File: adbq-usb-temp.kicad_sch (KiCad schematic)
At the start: 75 parts, among them J4 USB_C_Receptacle_USB2.0_14P, Q1 Q_NMOS, Q2 Q_NMOS, Q3 Q_NMOS, SW1 SW_Push, SW2 TestPoint, SW3 TestPoint, SW4 TestPoint, U1 ESP32-S3FH4R2, U14 TMP117AIDRV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

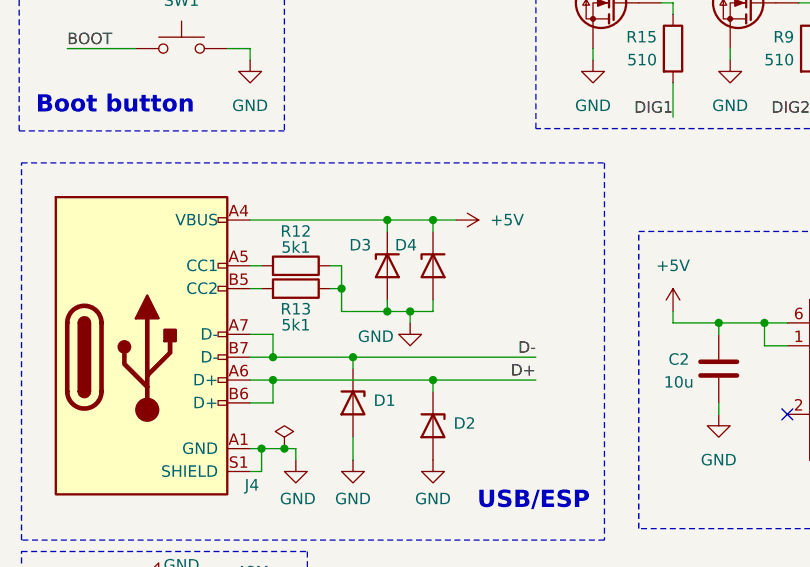
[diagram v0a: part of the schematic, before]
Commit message: pcb: add board outline
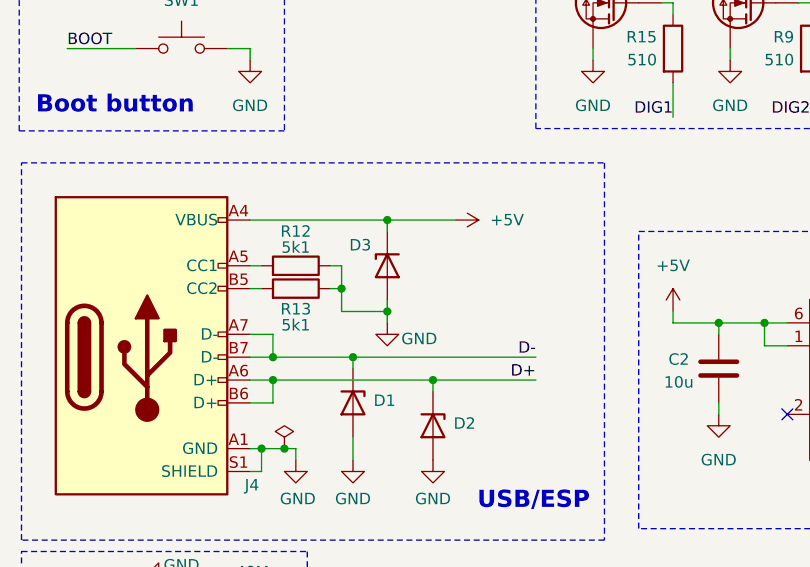
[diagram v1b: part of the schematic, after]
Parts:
- removed D4: H5VU10U, Pers:Diode_DFN1006, symbol Pers:H5VU10U
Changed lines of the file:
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@@
 	)
 	(junction
-		(at 62.23 135.89)
-		(diameter 0)
-		(color 0 0 0 0)
-	)
-	(junction
 		(at 148.59 158.75)
 		(diameter 0)
@@
 	)
 	(junction
-		(at 59.69 146.05)
-		(diameter 0)
-		(color 0 0 0 0)
-	)
-	(junction
 		(at 57.15 146.05)
 		(diameter 0)
@@
 	(wire
 		(pts
-			(xy 59.69 146.05) (xy 62.23 146.05)
-		)
-		(stroke
-			(width 0)
-			(type default)
-		)
-	)
-	(wire
-		(pts
 			(xy 45.72 161.29) (xy 46.99 161.29)
 		)
@@
 	(wire
 		(pts
-			(xy 59.69 147.32) (xy 59.69 146.05)
+			(xy 57.15 147.32) (xy 57.15 146.05)
 		)
 		(stroke
@@
 	(wire
 		(pts
-			(xy 57.15 146.05) (xy 59.69 146.05)
-		)
-		(stroke
-			(width 0)
-			(type default)
-		)
-	)
-	(wire
-		(pts
 			(xy 31.75 190.5) (xy 31.75 189.23)
 		)
@@
 	(wire
 		(pts
-			(xy 62.23 144.78) (xy 62.23 146.05)
-		)
-		(stroke
-			(width 0)
-			(type default)
-		)
-	)
-	(wire
-		(pts
-			(xy 62.23 135.89) (xy 62.23 137.16)
-		)
-		(stroke
-			(width 0)
-			(type default)
-		)
-	)
-	(wire
-		(pts
 			(xy 44.45 156.21) (xy 44.45 153.67)
 		)
@@
 	(wire
 		(pts
-			(xy 62.23 135.89) (xy 64.77 135.89)
-		)
-		(stroke
-			(width 0)
-			(type default)
-		)
-	)
-	(wire
-		(pts
 			(xy 172.72 38.1) (xy 182.88 38.1)
 		)
@@
 	(wire
 		(pts
-			(xy 57.15 135.89) (xy 62.23 135.89)
+			(xy 57.15 135.89) (xy 64.77 135.89)
 		)
 		(stroke
@@
 	)
 	(symbol
-		(lib_id "Pers:H5VU10U")
-		(at 62.23 140.97 90)
-		(mirror x)
-		(unit 1)
-		(exclude_from_sim no)
-		(in_bom yes)
-		(on_board yes)
-		(dnp no)
-		(property "Reference" "D4"
-			(at 60.452 138.684 90)
-			(effects
-				(font
-					(size 1.27 1.27)
-				)
-				(justify left)
-			)
-		)
-		(property "Value" "H5VU10U"
-			(at 59.69 142.2399 90)
-			(effects
-				(font
-					(size 1.27 1.27)
-				)
-				(justify left)
-				(hide yes)
-			)
-		)
-		(property "Footprint" "Pers:Diode_DFN1006"
-			(at 66.675 140.97 0)
-			(effects
-				(font
-					(size 1.27 1.27)
-				)
-				(hide yes)
-			)
-		)
-		(property "Datasheet" "https://datasheet.lcsc.com/lcsc/2504101957_hongjiacheng-H5VU10U_C22395519.pdf"
-			(at 62.23 140.97 0)
-			(effects
-				(font
-					(size 1.27 1.27)
-				)
-				(hide yes)
-			)
-		)
-		(property "Description" "-55℃~+155℃ 0.8pF 16V 200nA 55W@8/20us 5A@8/20us 5V 6V ESD IEC 61000-4-2 Unidirectional DFN1006-2L ESD and Surge Protection (TVS/ESD) ROHS"
-			(at 62.23 140.97 0)
-			(effects
-				(font
-					(size 1.27 1.27)
-				)
-				(hide yes)
-			)
-		)
-		(property "Basic" "E"
-			(at 62.23 140.97 90)
-			(effects
-				(font
-					(size 1.27 1.27)
-				)
-				(hide yes)
-			)
-		)
-		(property "JLCPCB Part #" "C22395519"
-			(at 62.23 140.97 90)
-			(effects
-				(font
-					(size 1.27 1.27)
-				)
-				(hide yes)
-			)
-		)
-		(property "Manufacturer" "hongjiacheng"
-			(at 62.23 140.97 90)
-			(effects
-				(font
-					(size 1.27 1.27)
-				)
-				(hide yes)
-			)
-		)
-		(property "Manufacturer Part Number" "H5VU10U"
-			(at 62.23 140.97 90)
-			(effects
-				(font
-					(size 1.27 1.27)
-				)
-				(hide yes)
-			)
-		)
-		(pin "1"
-		)
-		(pin "2"
-		)
-		(instances
-			(project "adbq-usb-temp"
-				(path "/683f6451-7bb7-4686-955a-dbaefe964302"
-					(reference "D4")
-					(unit 1)
-				)
-			)
-		)
-	)
-	(symbol
 		(lib_id "Switch:SW_Push")
 		(at 34.29 116.84 0)
@@
 	(symbol
 		(lib_id "power:GND")
-		(at 59.69 147.32 0)
+		(at 57.15 147.32 0)
 		(mirror y)
 		(unit 1)
@@
 		(dnp no)
 		(property "Reference" "#PWR029"
-			(at 59.69 153.67 0)
+			(at 57.15 153.67 0)
 			(effects
 				(font
@@
 		)
 		(property "Value" "GND"
-			(at 55.88 148.844 0)
+			(at 60.706 149.098 0)
 			(effects
 				(font
@@
 		)
 		(property "Footprint" ""
-			(at 59.69 147.32 0)
+			(at 57.15 147.32 0)
 			(effects
 				(font
@@
 		)
 		(property "Datasheet" ""
-			(at 59.69 147.32 0)
+			(at 57.15 147.32 0)
 			(effects
 				(font
@@
 		)
 		(property "Description" "Power symbol creates a global label with name \"GND\" , ground"
-			(at 59.69 147.32 0)
+			(at 57.15 147.32 0)
 			(effects
 				(font

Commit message: pcb: add SMPS routing
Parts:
- C2: footprint Capacitor_SMD:C_0402_1005Metric -> Capacitor_SMD:C_0603_1608Metric; JLCPCB Part # C15525 -> C19702; Manufacturer Part Number CL05A106MQ5NUNC -> CL10A106KP8NNNC
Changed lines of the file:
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@@
 			)
 		)
-		(property "Footprint" "Capacitor_SMD:C_0402_1005Metric"
+		(property "Footprint" "Capacitor_SMD:C_0603_1608Metric"
 			(at 94.9452 156.21 0)
 			(effects
@@
 			)
 		)
-		(property "JLCPCB Part #" "C15525"
+		(property "JLCPCB Part #" "C19702"
 			(at 93.98 152.4 0)
 			(effects
@@
 			)
 		)
-		(property "Manufacturer Part Number" "CL05A106MQ5NUNC"
+		(property "Manufacturer Part Number" "CL10A106KP8NNNC"
 			(at 93.98 152.4 0)
 			(effects

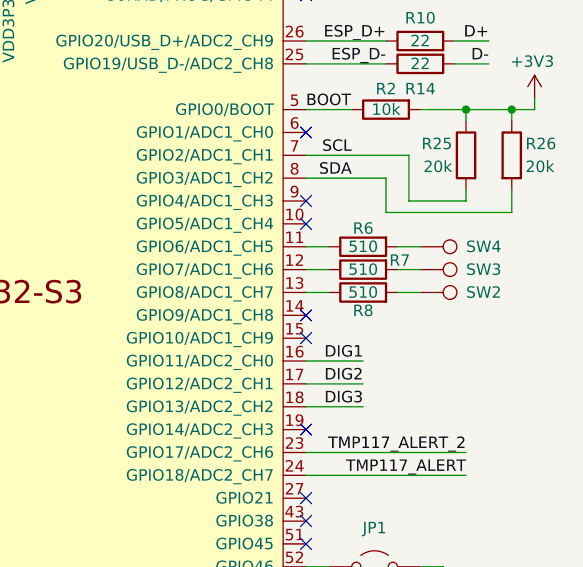
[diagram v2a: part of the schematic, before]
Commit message: pcb: add i2c routing
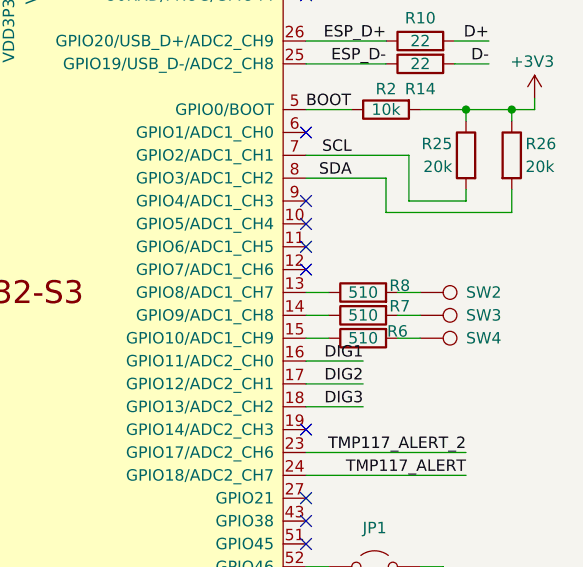
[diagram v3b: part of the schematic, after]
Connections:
- net at R6.1: now also U1.15 (GPIO10/ADC1_CH9); no longer U1.11 (GPIO6/ADC1_CH5)
- net at U1.12 (GPIO7/ADC1_CH6): no longer R7.1
- net at U1.14 (GPIO9/ADC1_CH8): now also R7.1
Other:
- moved on the sheet: R6, R7, SW3, SW4
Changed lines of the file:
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@@
 	)
 	(no_connect
-		(at 232.41 95.25)
-	)
-	(no_connect
 		(at 166.37 92.71)
 	)
@@
 	)
 	(no_connect
-		(at 232.41 97.79)
-	)
-	(no_connect
 		(at 166.37 123.19)
 	)
@@
 	)
 	(no_connect
+		(at 232.41 90.17)
+	)
+	(no_connect
 		(at 232.41 115.57)
 	)
 	(no_connect
+		(at 232.41 87.63)
+	)
+	(no_connect
 		(at 166.37 125.73)
 	)
@@
 	(wire
 		(pts
-			(xy 242.57 92.71) (xy 245.11 92.71)
+			(xy 232.41 95.25) (xy 234.95 95.25)
 		)
 		(stroke
@@
 	(wire
 		(pts
-			(xy 48.26 80.01) (xy 55.88 80.01)
+			(xy 242.57 92.71) (xy 245.11 92.71)
 		)
 		(stroke
@@
 	(wire
 		(pts
-			(xy 53.34 151.13) (xy 53.34 152.4)
+			(xy 48.26 80.01) (xy 55.88 80.01)
 		)
 		(stroke
@@
 	(wire
 		(pts
-			(xy 62.23 153.67) (xy 73.66 153.67)
+			(xy 53.34 151.13) (xy 53.34 152.4)
 		)
 		(stroke
@@
 	(wire
 		(pts
-			(xy 137.16 147.32) (xy 139.7 147.32)
+			(xy 62.23 153.67) (xy 73.66 153.67)
 		)
 		(stroke
@@
 	(wire
 		(pts
-			(xy 129.54 160.02) (xy 129.54 157.48)
+			(xy 137.16 147.32) (xy 139.7 147.32)
 		)
 		(stroke
@@
 	(wire
 		(pts
-			(xy 232.41 90.17) (xy 234.95 90.17)
+			(xy 129.54 160.02) (xy 129.54 157.48)
 		)
 		(stroke
@@
 	(wire
 		(pts
+			(xy 242.57 97.79) (xy 245.11 97.79)
+		)
+		(stroke
+			(width 0)
+			(type default)
+		)
+	)
+	(wire
+		(pts
 			(xy 152.4 107.95) (xy 153.67 107.95)
 		)
@@
 	(wire
 		(pts
-			(xy 242.57 90.17) (xy 245.11 90.17)
-		)
-		(stroke
-			(width 0)
-			(type default)
-		)
-	)
-	(wire
-		(pts
 			(xy 137.16 44.45) (xy 142.24 44.45)
 		)
@@
 	(wire
 		(pts
-			(xy 242.57 87.63) (xy 245.11 87.63)
-		)
-		(stroke
-			(width 0)
-			(type default)
-		)
-	)
-	(wire
-		(pts
 			(xy 41.91 135.89) (xy 57.15 135.89)
 		)
@@
 	(wire
 		(pts
+			(xy 242.57 95.25) (xy 245.11 95.25)
+		)
+		(stroke
+			(width 0)
+			(type default)
+		)
+	)
+	(wire
+		(pts
 			(xy 36.83 185.42) (xy 36.83 186.69)
 		)
@@
 	(wire
 		(pts
-			(xy 232.41 87.63) (xy 234.95 87.63)
-		)
-		(stroke
-			(width 0)
-			(type default)
-		)
-	)
-	(wire
-		(pts
 			(xy 243.84 77.47) (xy 243.84 82.55)
 		)
@@
 	(wire
 		(pts
+			(xy 232.41 97.79) (xy 234.95 97.79)
+		)
+		(stroke
+			(width 0)
+			(type default)
+		)
+	)
+	(wire
+		(pts
 			(xy 166.37 107.95) (xy 161.29 107.95)
 		)
@@
 	(symbol
 		(lib_id "Connector:TestPoint")
-		(at 245.11 90.17 270)
+		(at 245.11 95.25 270)
 		(unit 1)
 		(exclude_from_sim no)
@@
 		(dnp no)
 		(property "Reference" "SW3"
-			(at 250.19 90.17 90)
+			(at 250.19 95.25 90)
 			(effects
 				(font
@@
 		)
 		(property "Value" "TestPoint"
-			(at 250.19 91.4399 90)
+			(at 250.19 96.5199 90)
 			(effects
 				(font
@@
 		)
 		(property "Footprint" "TestPoint:TestPoint_Pad_D1.5mm"
-			(at 245.11 95.25 0)
+			(at 245.11 100.33 0)
 			(effects
 				(font
@@
 		)
 		(property "Datasheet" "~"
-			(at 245.11 95.25 0)
+			(at 245.11 100.33 0)
 			(effects
 				(font
@@
 		)
 		(property "Description" "test point"
-			(at 245.11 90.17 0)
+			(at 245.11 95.25 0)
 			(effects
 				(font
@@
 	(symbol
 		(lib_id "Connector:TestPoint")
-		(at 245.11 87.63 270)
+		(at 245.11 97.79 270)
 		(unit 1)
 		(exclude_from_sim no)
@@
 		(dnp no)
 		(property "Reference" "SW4"
-			(at 250.19 87.63 90)
+			(at 250.19 97.79 90)
 			(effects
 				(font
@@
 		)
 		(property "Value" "TestPoint"
-			(at 250.19 88.8999 90)
+			(at 250.19 99.0599 90)
 			(effects
 				(font
@@
 		)
 		(property "Footprint" "TestPoint:TestPoint_Pad_D1.5mm"
-			(at 245.11 92.71 0)
+			(at 245.11 102.87 0)
 			(effects
 				(font
@@
 		)
 		(property "Datasheet" "~"
-			(at 245.11 92.71 0)
+			(at 245.11 102.87 0)
 			(effects
 				(font
@@
 		)
 		(property "Description" "test point"
-			(at 245.11 87.63 0)
+			(at 245.11 97.79 0)
 			(effects
 				(font
@@
 		(dnp no)
 		(property "Reference" "R8"
-			(at 238.76 94.742 90)
+			(at 242.824 91.948 90)
 			(effects
 				(font
@@
 	(symbol
 		(lib_id "Device:R")
-		(at 238.76 87.63 90)
+		(at 238.76 97.79 90)
 		(mirror x)
 		(unit 1)
@@
 		(dnp no)
 		(property "Reference" "R6"
-			(at 238.76 85.598 90)
+			(at 242.57 97.028 90)
 			(effects
 				(font
@@
 		)
 		(property "Value" "510"
-			(at 238.76 87.63 90)
+			(at 238.76 97.79 90)
 			(effects
 				(font
@@
 		)
 		(property "Footprint" "Resistor_SMD:R_0402_1005Metric"
-			(at 238.76 85.852 90)
+			(at 238.76 96.012 90)
 			(effects
 				(font
@@
 		)
 		(property "Datasheet" "~"
-			(at 238.76 87.63 0)
+			(at 238.76 97.79 0)
 			(effects
 				(font
@@
 		)
 		(property "Description" "Resistor"
-			(at 238.76 87.63 0)
+			(at 238.76 97.79 0)
 			(effects
 				(font
@@
 		)
 		(property "Basic" "Y"
-			(at 238.76 87.63 90)
+			(at 238.76 97.79 90)
 			(effects
 				(font
@@
 		)
 		(property "JLCPCB Part #" "C25123"
-			(at 238.76 87.63 90)
+			(at 238.76 97.79 90)
 			(effects
 				(font
@@
 		)
 		(property "Manufacturer" "Uniroyal Elec"
-			(at 238.76 87.63 90)
+			(at 238.76 97.79 90)
 			(effects
 				(font
@@
 		)
 		(property "Manufacturer Part Number" "0402WGF5100TCE"
-			(at 238.76 87.63 90)
+			(at 238.76 97.79 90)
 			(effects
 				(font
@@
 		)
 		(instances
-			(project ""
+			(project "adbq-usb-temp"
 				(path "/683f6451-7bb7-4686-955a-dbaefe964302"
 					(reference "R6")
@@
 	(symbol
 		(lib_id "Device:R")
-		(at 238.76 90.17 90)
+		(at 238.76 95.25 90)
 		(mirror x)
 		(unit 1)
@@
 		(dnp no)
 		(property "Reference" "R7"
-			(at 242.824 89.154 90)
+			(at 242.824 94.234 90)
 			(effects
 				(font
@@
 		)
 		(property "Value" "510"
-			(at 238.76 90.17 90)
+			(at 238.76 95.25 90)
 			(effects
 				(font
@@
 		)
 		(property "Footprint" "Resistor_SMD:R_0402_1005Metric"
-			(at 238.76 88.392 90)
+			(at 238.76 93.472 90)
 			(effects
 				(font
@@
 		)
 		(property "Datasheet" "~"
-			(at 238.76 90.17 0)
+			(at 238.76 95.25 0)
 			(effects
 				(font
@@
 		)
 		(property "Description" "Resistor"
-			(at 238.76 90.17 0)
+			(at 238.76 95.25 0)
 			(effects
 				(font
@@
 		)
 		(property "Basic" "Y"
-			(at 238.76 90.17 90)
+			(at 238.76 95.25 90)
 			(effects
 				(font
@@
 		)
 		(property "JLCPCB Part #" "C25123"
-			(at 238.76 90.17 90)
+			(at 238.76 95.25 90)
 			(effects
 				(font
@@
 		)
 		(property "Manufacturer" "Uniroyal Elec"
-			(at 238.76 90.17 90)
+			(at 238.76 95.25 90)
 			(effects
 				(font
@@
 		)
 		(property "Manufacturer Part Number" "0402WGF5100TCE"
-			(at 238.76 90.17 90)
+			(at 238.76 95.25 90)
 			(effects
 				(font

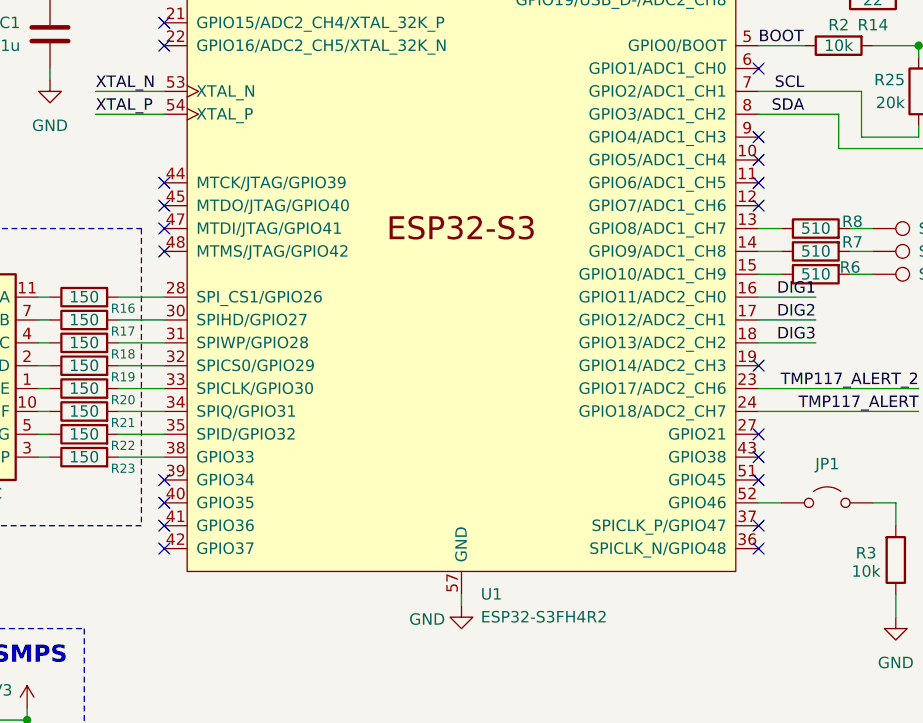
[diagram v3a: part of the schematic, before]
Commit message: pcb: add segment display routing
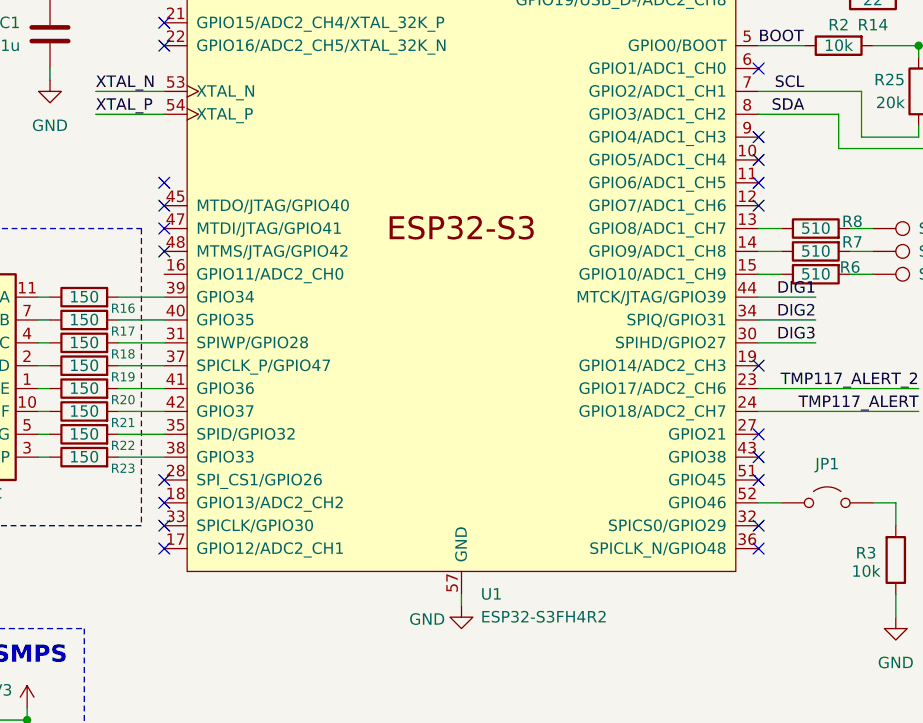
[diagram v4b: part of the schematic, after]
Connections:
- net DIG1: now also U1.44 (MTCK/JTAG/GPIO39); no longer U1.16 (GPIO11/ADC2_CH0)
- net DIG2: now also U1.34 (SPIQ/GPIO31); no longer U1.17 (GPIO12/ADC2_CH1)
- net DIG3: now also U1.30 (SPIHD/GPIO27); no longer U1.18 (GPIO13/ADC2_CH2)
- net at R16.2: now also U1.39 (GPIO34); no longer U1.28 (SPI_CS1/GPIO26)
- net at R17.2: now also U1.40 (GPIO35); no longer U1.30 (SPIHD/GPIO27)
- net at R20.2: now also U1.41 (GPIO36); no longer U1.33 (SPICLK/GPIO30)
- net at R19.2: now also U1.37 (SPICLK_P/GPIO47); no longer U1.32 (SPICS0/GPIO29)
- net at R21.2: now also U1.42 (GPIO37); no longer U1.34 (SPIQ/GPIO31)
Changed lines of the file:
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@@
 		(on_board yes)
 		(dnp no)
-		(fields_autoplaced yes)
 		(property "Reference" "U1"
 			(at 201.5333 133.35 0)

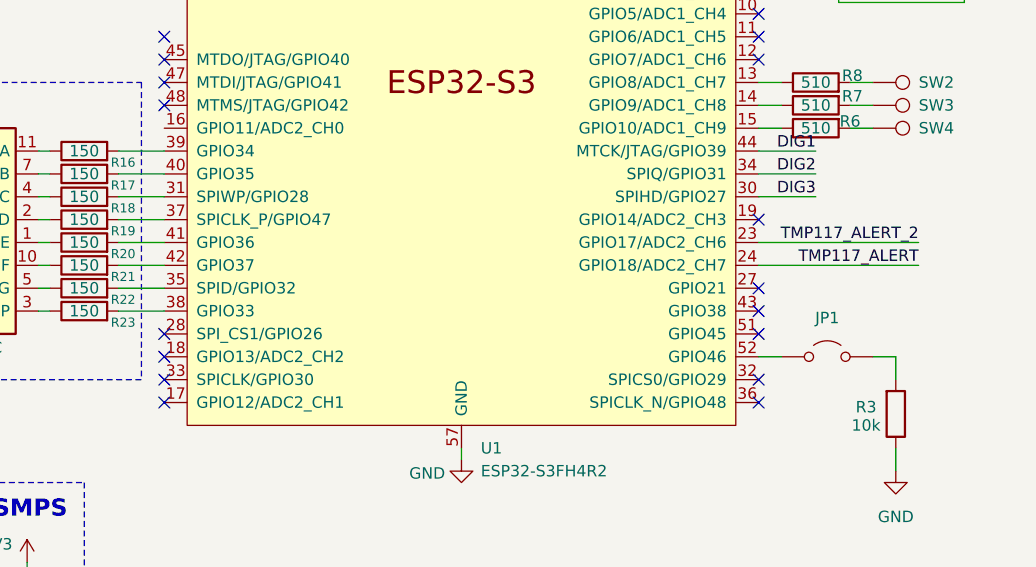
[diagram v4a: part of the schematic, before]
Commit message: pcb: add TMP117 routing
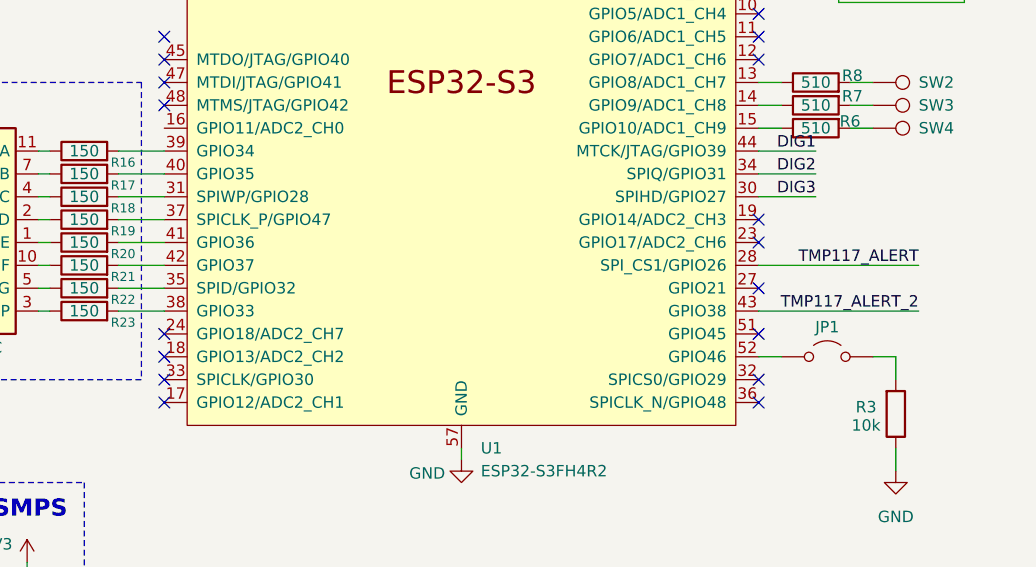
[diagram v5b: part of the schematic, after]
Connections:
- net TMP117_ALERT: now also U1.28 (SPI_CS1/GPIO26); no longer U1.24 (GPIO18/ADC2_CH7)
- net TMP117_ALERT_2: now also U1.43 (GPIO38); no longer U1.23 (GPIO17/ADC2_CH6)
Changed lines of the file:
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@@
 	)
 	(no_connect
-		(at 232.41 118.11)
-	)
-	(no_connect
 		(at 232.41 74.93)
 	)
@@
 	)
 	(no_connect
+		(at 232.41 110.49)
+	)
+	(no_connect
 		(at 166.37 90.17)
 	)
@@
 	(wire
 		(pts
+			(xy 232.41 118.11) (xy 250.19 118.11)
+		)
+		(stroke
+			(width 0)
+			(type default)
+		)
+	)
+	(wire
+		(pts
 			(xy 172.72 38.1) (xy 182.88 38.1)
 		)
@@
 	(wire
 		(pts
-			(xy 232.41 110.49) (xy 250.19 110.49)
-		)
-		(stroke
-			(width 0)
-			(type default)
-		)
-	)
-	(wire
-		(pts
 			(xy 53.34 151.13) (xy 73.66 151.13)
 		)
@@
 		)
 	)
-	(label "TMP117_ALERT_2"
-		(at 250.19 110.49 180)
-		(effects
-			(font
-				(size 1.27 1.27)
-			)
-			(justify right bottom)
-		)
-	)
 	(label "DIG1"
 		(at 88.9 124.46 180)
@@
 		)
 	)
+	(label "TMP117_ALERT_2"
+		(at 250.19 118.11 180)
+		(effects
+			(font
+				(size 1.27 1.27)
+			)
+			(justify right bottom)
+		)
+	)
 	(label "SCL"
 		(at 237.49 77.47 180)
@@
 		(dnp no)
 		(property "Reference" "JP1"
-			(at 240.03 118.872 0)
+			(at 240.03 119.888 0)
 			(effects
 				(font

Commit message: pcb: clean tracks
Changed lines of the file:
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@@
-	)
-	(no_connect
-		(at 166.37 87.63)
 	)
 	(no_connect
@@
 	)
 	(no_connect
+		(at 166.37 97.79)
+	)
+	(no_connect
